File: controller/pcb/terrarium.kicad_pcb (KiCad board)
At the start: 2 copper layers, 90 x 90 mm, 66 parts, among them Q1 S8050, Q2 S8050, Q3 S8050, Q4 S8050, SW1 RESET, SW3 RTC BATTERY, U1 ESP32-WROOM-32, U2 DS3231M, U3 LM1117-3.3

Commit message: wip, added all footprints
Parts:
- removed RE1, RE2, RE3: SANYOU_SRD_Form_C, Relay_THT:Relay_SPDT_SANYOU_SRD_Series_Form_C
- added K1: G3MB-202P, Omron:RELAY_G3MB-202P, F.Cu at (147.6, 91.1)
- added K2: G3MB-202P, Omron:RELAY_G3MB-202P, F.Cu at (147.6, 98.7)
- added K3: G3MB-202P, Omron:RELAY_G3MB-202P, F.Cu at (147.6, 106.3)
- added P1: USB_C_Plug_USB2.0, Connector_USB:USB_C_Receptacle_Palconn_UTC16-G, F.Cu at (166.7, 99.2)
- added R18: 1M, Resistor_SMD:R_1206_3216Metric, F.Cu at (163.7, 106.7)
- added UART2: Nextion, Connector_JST:JST_XH_B4B-XH-AM_1x04_P2.50mm_Vertical, F.Cu at (164.4, 90.6)
- renumbered UART to UART1

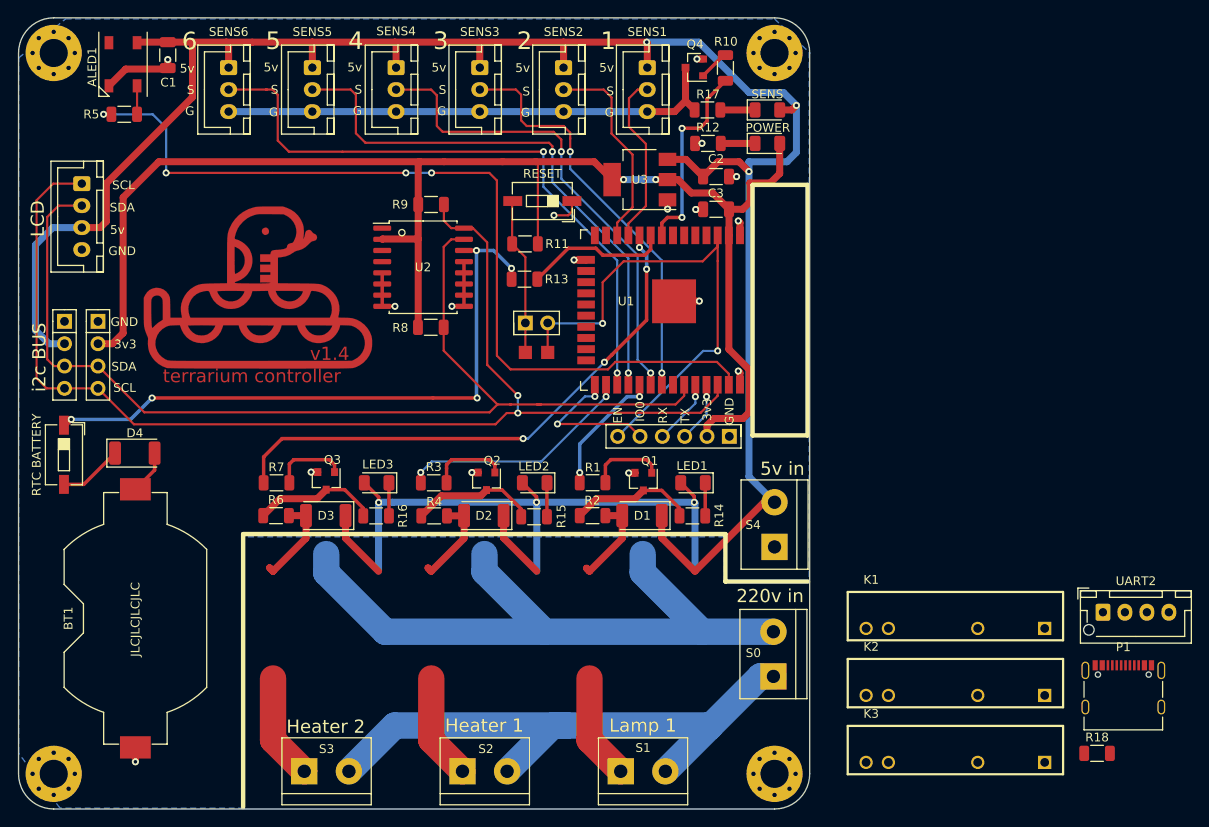
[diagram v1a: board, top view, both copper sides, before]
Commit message: place components for v1.5
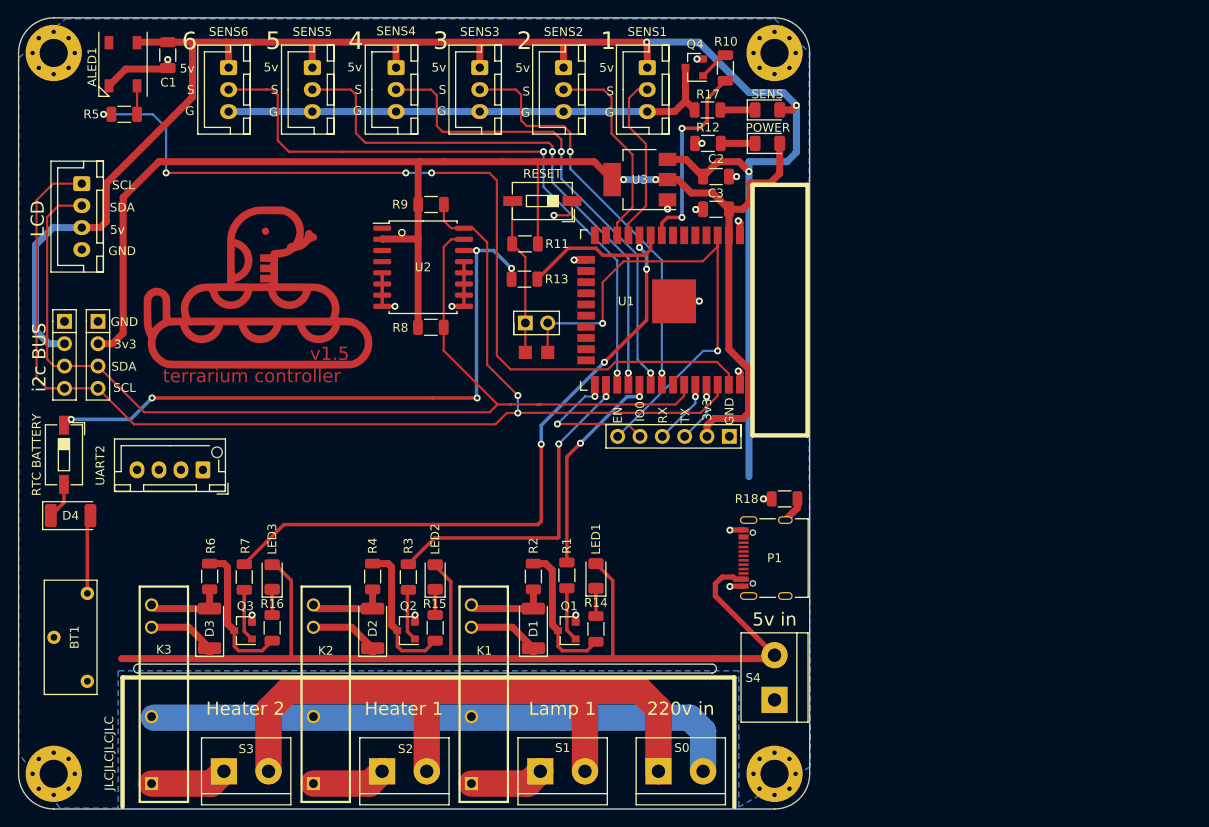
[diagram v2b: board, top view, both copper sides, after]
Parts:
- BT1: footprint Battery:BatteryHolder_Keystone_1058_1x2032 -> Custom_Battery:CR2032_vertical
- moved UART2 103.7 mm to (62.0, 74.4), turned to 180 degrees
- moved K3 90.3 mm to (57.5, 99.9), turned to 270 degrees
- moved K2 71.6 mm to (75.9, 99.9), turned to 270 degrees
- moved K1 54.4 mm to (93.9, 99.9), turned to 270 degrees
- moved R18 45.8 mm to (128.1, 77.7), turned to 180 degrees
- moved P1 43.3 mm to (126.0, 84.5), turned to 90 degrees
- moved Q3 19.5 mm to (66.5, 92.7), turned to 180 degrees
- moved Q2 19.3 mm to (85.1, 92.7), turned to 180 degrees
- moved Q1 19.1 mm to (103.4, 92.7), turned to 180 degrees
- moved D3 18.4 mm to (62.7, 92.5), turned to 90 degrees
- moved D2 18.0 mm to (81.3, 92.5), turned to 90 degrees
- moved D1 17.8 mm to (99.6, 92.5), turned to 90 degrees
- moved S4 17.4 mm to (127.0, 100.6)
- moved R16 17.4 mm to (69.8, 92.4), turned to 270 degrees
- moved S0 17.0 mm to (113.8, 108.7), turned to 0 degrees
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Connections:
- K1 pad 1: 220L -> Net-(K1-Pad1)
- K1 pad 2: Net-(K1-Pad2) -> 220L
- K2 pad 1: 220L -> Net-(K2-Pad1)
- K2 pad 2: Net-(K2-Pad2) -> 220L
- K3 pad 1: 220L -> Net-(K3-Pad1)
- K3 pad 2: Net-(K3-Pad2) -> 220L
- S1 pad 1: Net-(K1-Pad2) -> Net-(K1-Pad1)
- S2 pad 1: Net-(K2-Pad2) -> Net-(K2-Pad1)
- S3 pad 1: Net-(K3-Pad2) -> Net-(K3-Pad1)
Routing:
- net +5V: track 312.0 -> 354.7 mm, vias 6 -> 3
- net Net-(K3-Pad2): track 12.0 -> 0.00 mm
- net Net-(K2-Pad2): track 12.0 -> 0.00 mm
- net Net-(K1-Pad2): track 12.0 -> 0.00 mm
- net 220L: track 79.1 -> 67.7 mm
- net G4: track 27.2 -> 37.9 mm
- net G25: track 62.9 -> 73.6 mm
- net 220N: track 69.0 -> 79.0 mm
- net G5: track 14.8 -> 24.6 mm
- net Net-(K3-Pad1): track 0.00 -> 8.80 mm
- net Net-(K1-Pad1): track 0.00 -> 8.42 mm
- net Net-(K2-Pad1): track 0.00 -> 8.39 mm
- net Net-(BT1-Pad1): track 5.02 -> 8.99 mm
- net Net-(D4-Pad1): track 7.29 -> 4.17 mm
- net Net-(P1-PadS1): track 0.00 -> 2.98 mm
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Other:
- outline, holes or cut-outs redrawn
- board text added: "v1.5"
- board text removed: "v1.4"

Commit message: almost done
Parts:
- removed i2c2: LCD, Connector_JST:JST_XH_B4B-XH-AM_1x04_P2.50mm_Vertical
- removed i2c3: Extra_5v, Connector_PinHeader_2.54mm:PinHeader_1x04_P2.54mm_Vertical
- removed i2c4: Extra_3v3, Connector_PinHeader_2.54mm:PinHeader_1x04_P2.54mm_Vertical
- added I2C1: 1, Connector_JST:JST_XH_B4B-XH-AM_1x04_P2.50mm_Vertical, F.Cu at (46.0, 67.0)
- added I2C2: 4, Connector_JST:JST_XH_B4B-XH-AM_1x04_P2.50mm_Vertical, F.Cu at (46.0, 60.0)
- added I2C3: 3, Connector_JST:JST_XH_B4B-XH-AM_1x04_P2.50mm_Vertical, F.Cu at (46.0, 53.0)
- added I2C4: 2, Connector_JST:JST_XH_B4B-XH-AM_1x04_P2.50mm_Vertical, F.Cu at (46.0, 46.0)
- added I2C5: 5, Connector_JST:JST_XH_B4B-XH-AM_1x04_P2.50mm_Vertical, F.Cu at (46.0, 39.0)
- added LED6: RX, LED_SMD:LED_1206_3216Metric, F.Cu at (113.0, 85.2)
- added LED7: TX, LED_SMD:LED_1206_3216Metric, F.Cu at (113.0, 87.8)
- added R19: 10k, Resistor_SMD:R_1206_3216Metric, F.Cu at (113.0, 82.8)
- moved SW3 64.3 mm to (110.5, 71.1), turned to 180 degrees
- moved D4 63.7 mm to (110.5, 75.6), turned to 180 degrees
- moved SW1 39.4 mm to (126.1, 73.8)
- moved R11 38.2 mm to (123.8, 77.5)
- moved RESET_j1 35.4 mm to (110.9, 90.9)
- moved TP1 35.2 mm to (113.4, 94.1), turned to 0 degrees
- moved TP2 35.2 mm to (110.9, 94.1), turned to 0 degrees
- moved UART1 22.7 mm to (117.2, 92.8), turned to 180 degrees
- moved UART2 16.0 mm to (46.0, 74.0), turned to 0 degrees
- moved R13 11.3 mm to (104.8, 43.4), turned to 90 degrees
- moved R9 10.0 mm to (96.7, 49.1)
- moved U2 10.0 mm to (95.8, 56.2)
- moved R8 10.0 mm to (96.7, 63.0)
- moved G*** 5.35 mm to (73.6, 53.3)
- moved R5 5.03 mm to (58.0, 33.6), turned to 90 degrees
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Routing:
- net TX: track 6.90 -> 108.1 mm, vias 1 -> 0
- net RX: track 8.07 -> 98.7 mm, vias 1 -> 0
- net Net-(BT1-Pad1): track 8.99 -> 68.2 mm, vias 0 -> 2
- net +3V3: track 167.4 -> 120.8 mm
- net +5V: track 354.7 -> 384.0 mm, vias 3 -> 4
- net Net-(R13-Pad2): track 72.6 -> 49.4 mm, vias 5 -> 3
- net G23: track 100.9 -> 81.2 mm, vias 4 -> 2
- net Net-(R11-Pad2): track 17.9 -> 32.0 mm, vias 0 -> 2
- net IO0: track 16.9 -> 27.2 mm, vias 2 -> 1
- net SCL: track 138.6 -> 130.1 mm, vias 2 -> 6
- net EN: track 58.9 -> 52.7 mm
- net Net-(LED6-Pad1): track 0.00 -> 4.97 mm
- net SDA: track 121.3 -> 125.5 mm, vias 0 -> 2
- net G25: track 73.6 -> 77.2 mm
- net Net-(D4-Pad1): track 4.17 -> 7.46 mm
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- added copper zone on F.Cu, net GND
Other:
- board text removed: "LCD"
- board text removed: "i2c BUS"

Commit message: update footprints, move rx/tx leds
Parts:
- removed R19: 10k, Resistor_SMD:R_1206_3216Metric
- removed SW3: RTC BATTERY, Button_Switch_SMD:SW_DIP_SPSTx01_Slide_6.7x4.1mm_W6.73mm_P2.54mm_LowProfile_JPin
- LED4: value POWER -> PWR
- LED5: value SENS -> SNS
- R12: value 5k -> 3k
- moved D4 59.4 mm to (52.1, 86.2), turned to 270 degrees
- moved LED7 52.9 mm to (128.4, 37.1)
- moved LED6 52.9 mm to (128.4, 34.6)
- moved TP1 27.6 mm to (122.7, 68.1)
- moved TP2 26.8 mm to (122.7, 70.0)
- moved RESET_j1 18.1 mm to (117.2, 73.9), turned to 0 degrees
- moved LED4 3.24 mm to (128.4, 39.7)
- moved LED5 2.56 mm to (128.4, 32.2)
- moved R12 0.08 mm to (120.5, 37.2)
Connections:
- LED4 pad 1: Net-(LED4-Pad1) -> GND
- LED4 pad 2: +3V3 -> Net-(LED4-Pad2)
- LED6 pad 1: Net-(LED6-Pad1) -> RX
- LED6 pad 2: RX -> Net-(LED4-Pad2)
- LED7 pad 1: Net-(LED6-Pad1) -> TX
- LED7 pad 2: TX -> Net-(LED4-Pad2)
- R12 pad 1: GND -> +3V3
- R12 pad 2: Net-(LED4-Pad1) -> Net-(LED4-Pad2)
- R13 pad 2: Net-(R13-Pad2) -> Net-(D4-Pad1)
- U2 pad 14: Net-(R13-Pad2) -> Net-(D4-Pad1)
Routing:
- net Net-(D4-Pad1): track 7.46 -> 97.9 mm, vias 0 -> 3
- net Net-(BT1-Pad1): track 68.2 -> 3.26 mm, vias 2 -> 0
- net Net-(R13-Pad2): track 49.4 -> 0.00 mm, vias 3 -> 0
- net RX: track 98.7 -> 133.3 mm, vias 0 -> 2
- net TX: track 108.1 -> 137.6 mm, vias 0 -> 2
- net Net-(P1-PadS1): track 3.88 -> 20.9 mm
- net Net-(LED4-Pad2): track 0.00 -> 14.9 mm
- net Net-(R11-Pad2): track 32.0 -> 21.9 mm, vias 2 -> 3
- net EN: track 52.7 -> 45.4 mm
- net Net-(LED6-Pad1): track 4.97 -> 0.00 mm
- net +3V3: track 120.8 -> 115.9 mm, vias 2 -> 3
- net G26: track 20.6 -> 24.7 mm
- net GND: track 43.4 -> 39.6 mm, vias 31 -> 38
- net Net-(LED4-Pad1): track 2.87 -> 0.00 mm
- net Net-(LED5-Pad1): track 2.87 -> 5.61 mm
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
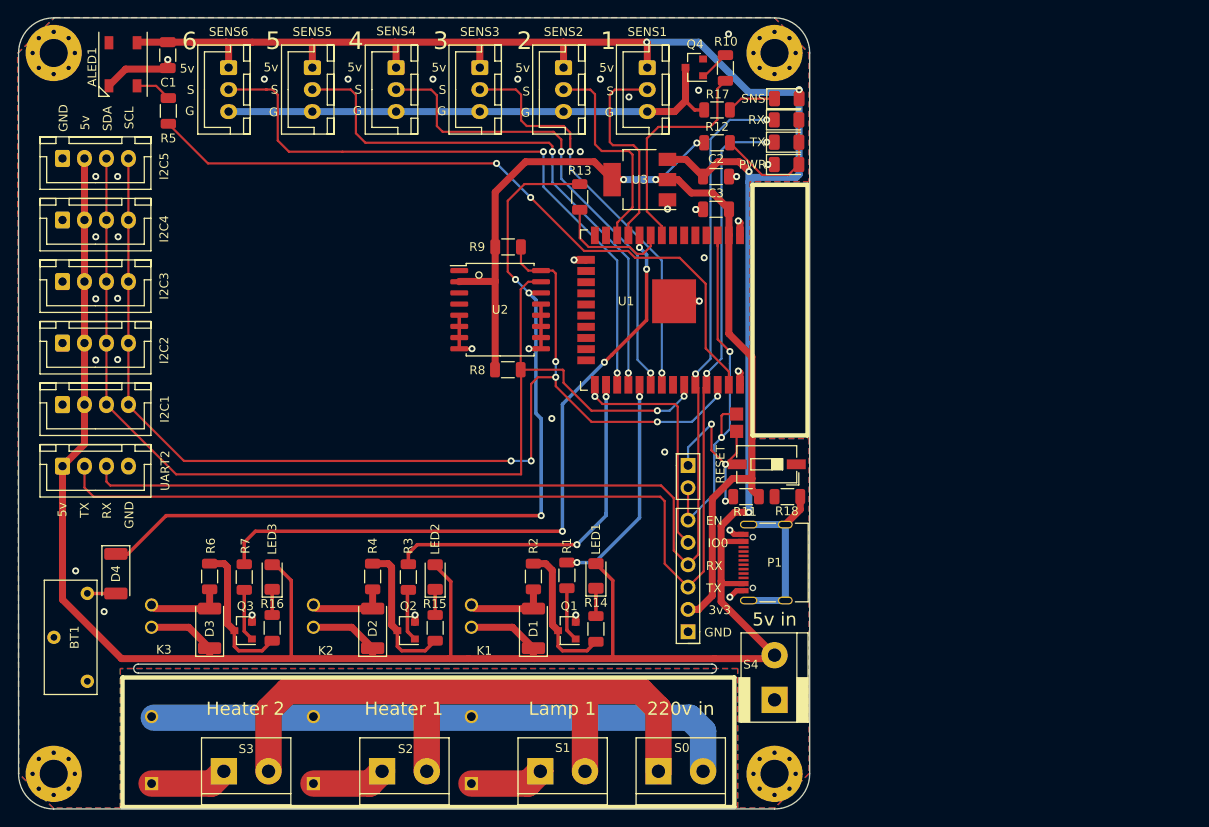
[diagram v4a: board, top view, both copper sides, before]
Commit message: add cp2102
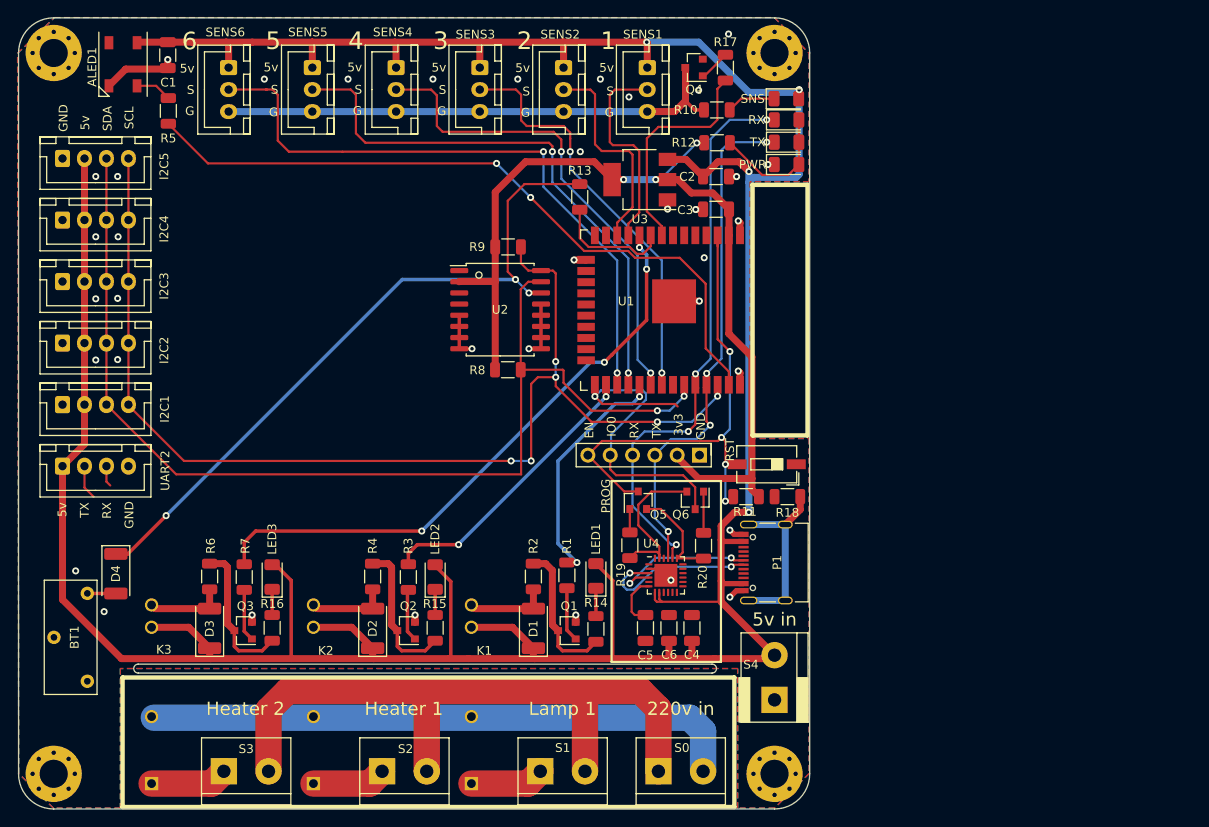
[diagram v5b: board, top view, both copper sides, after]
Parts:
- removed RESET_j1: data, Connector_PinHeader_2.54mm:PinHeader_1x02_P2.54mm_Vertical
- removed TP1, TP2: TestPoint, TestPoint:TestPoint_Pad_1.5x1.5mm
- added C4: 4.7uF, Capacitor_SMD:C_1206_3216Metric, F.Cu at (117.6, 92.4)
- added C5: 100nF, Capacitor_SMD:C_1206_3216Metric, F.Cu at (112.3, 92.4)
- added C6: 100nF, Capacitor_SMD:C_1206_3216Metric, F.Cu at (115.0, 92.4)
- added Q5: BC817, Package_TO_SOT_SMD:SOT-23, F.Cu at (111.5, 77.9)
- added Q6: BC817, Package_TO_SOT_SMD:SOT-23, F.Cu at (118.0, 77.9)
- added R19: 10k, Resistor_SMD:R_1206_3216Metric, F.Cu at (110.5, 83.0)
- added R20: 10k, Resistor_SMD:R_1206_3216Metric, F.Cu at (118.9, 83.0)
- added U4: CP2102N-A01-GQFN24, Package_DFN_QFN:QFN-24-1EP_4x4mm_P0.5mm_EP2.6x2.6mm, F.Cu at (114.6, 86.4)
- R10: value 150ohm -> 5k
- R17: value 5k -> 150ohm
- SENS1: value 4 -> 1
- SENS2: value 4 -> 2
- SENS3: value 1 -> 3
- SENS4: value 2 -> 4
- SENS5: value 3 -> 4
- SW1: value RESET -> RST
- moved UART1 20.1 mm to (118.5, 72.7), turned to 270 degrees
- moved R17 4.91 mm to (121.4, 28.7), turned to 90 degrees
- moved R10 4.87 mm to (120.4, 33.5), turned to 180 degrees
- moved LED5 0.06 mm to (128.3, 32.2)
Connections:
- R10 pad 1: G32 -> Net-(LED5-Pad1)
- R10 pad 2: Net-(Q4-Pad1) -> Net-(Q4-Pad3)
- R11 pad 2: Net-(R11-Pad2) -> EN
- R17 pad 1: Net-(LED5-Pad1) -> G32
- R17 pad 2: Net-(Q4-Pad3) -> Net-(Q4-Pad1)
- SW1 pad 2: Net-(R11-Pad2) -> EN
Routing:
- net TX: track 137.6 -> 63.0 mm, vias 2 -> 4
- net RX: track 133.3 -> 67.9 mm, vias 2 -> 4
- net Net-(R11-Pad2): track 21.9 -> 0.00 mm, vias 3 -> 0
- net Net-(P1-PadA6): track 0.00 -> 19.0 mm, vias 0 -> 2
- net Net-(D4-Pad1): track 97.9 -> 80.2 mm
- net Net-(Q6-Pad2): track 0.00 -> 17.4 mm
- net Net-(P1-PadA7): track 0.00 -> 16.7 mm, vias 0 -> 2
- net +5V: track 386.2 -> 399.9 mm
- net IO0: track 27.2 -> 40.8 mm
- net EN: track 45.4 -> 58.5 mm, vias 2 -> 4
- net Net-(Q5-Pad2): track 0.00 -> 11.6 mm
- net +3V3: track 115.9 -> 105.8 mm
- net G25: track 77.2 -> 68.7 mm
- net G4: track 40.4 -> 32.5 mm
- net Net-(C5-Pad1): track 0.00 -> 6.02 mm
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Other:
- board text added: "PROG"

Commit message: add ground, 5v inner planes
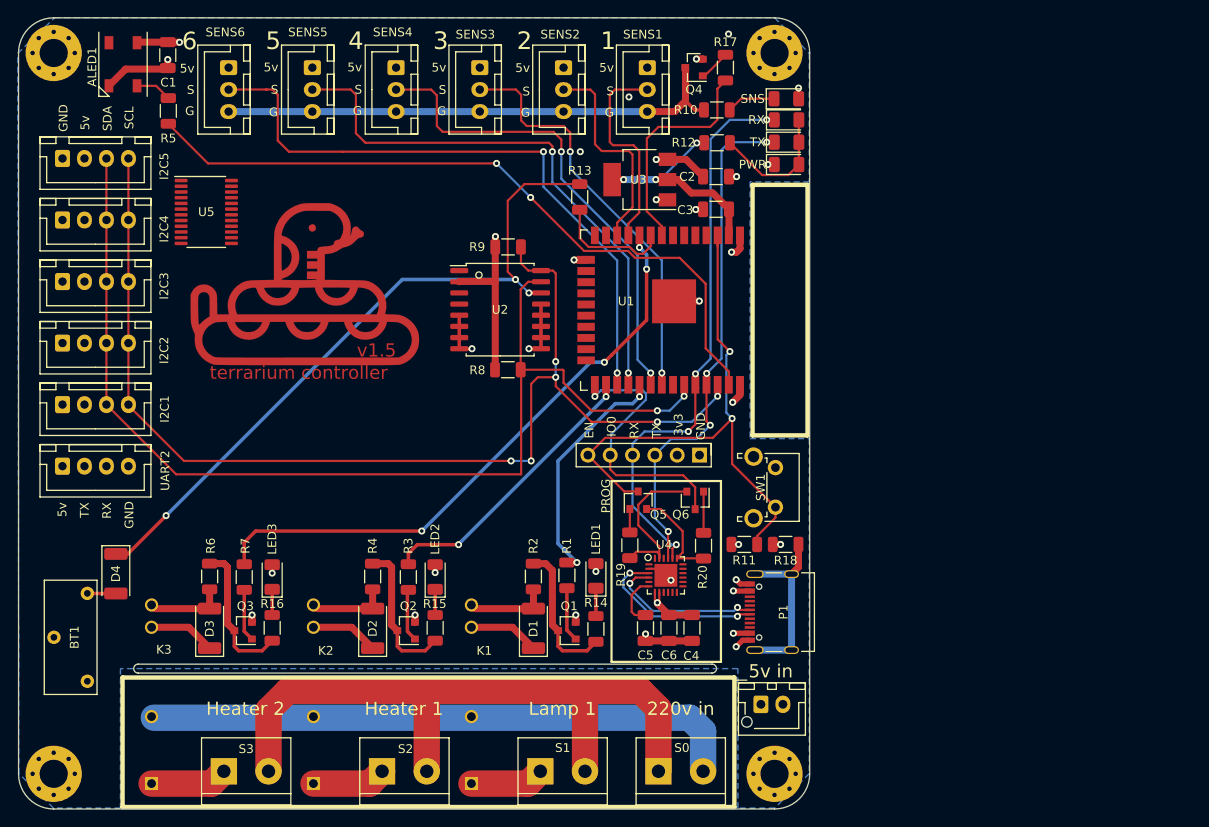
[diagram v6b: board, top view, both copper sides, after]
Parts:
- added U5: TCA9548APWR, Package_SO:TSSOP-24_4.4x7.8mm_P0.65mm, F.Cu at (62.4, 45.1)
- S4: value 5v in -> PWR; footprint TerminalBlock:TerminalBlock_bornier-2_P5.08mm -> Connector_JST:JST_XH_B2B-XH-AM_1x02_P2.50mm_Vertical
- SW1: footprint Button_Switch_SMD:SW_DIP_SPSTx01_Slide_6.7x4.1mm_W6.73mm_P2.54mm_LowProfile_JPin -> Button_Switch_THT:SW_Tactile_SPST_Angled_PTS645Vx39-2LFS
- moved P1 5.68 mm to (126.7, 90.6)
- moved R11 5.44 mm to (123.6, 82.9), turned to 0 degrees
- moved R18 5.44 mm to (128.3, 82.9)
- moved S4 1.63 mm to (125.5, 101.1), turned to 0 degrees
- moved SW1 1.06 mm to (127.1, 74.2), turned to 270 degrees
- turned C4 to 270 degrees
- turned C6 to 270 degrees
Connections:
- S4 pad 1: GND -> +5V
- S4 pad 2: +5V -> GND
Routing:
- net +5V: track 399.9 -> 50.2 mm, vias 4 -> 9
- net +3V3: track 105.8 -> 45.3 mm, vias 3 -> 5
- net IO0: track 40.8 -> 30.9 mm
- net GND: track 41.8 -> 51.4 mm, vias 37 -> 23
- net EN: track 58.5 -> 65.9 mm, vias 4 -> 2
- net TX: track 63.0 -> 59.1 mm
- net RX: track 67.9 -> 65.5 mm
- net Net-(P1-PadA7): track 16.7 -> 18.0 mm
- net Net-(P1-PadA6): track 19.0 -> 19.9 mm
- added copper zone on B.Cu, net +3V3
- added copper zone on In2.Cu, net +5V
- added copper zone on In1.Cu, net GND
- removed copper zone on B.Cu, net GND
- removed copper zone on F.Cu, net GND
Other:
- copper layers 2 -> 4
